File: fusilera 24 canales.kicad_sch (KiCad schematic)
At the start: 25 parts, among them Q2 MMBT2222A, Q3 MMBT2222A, U4 74HC132D, U5 LM339D, U6 BTS50010-1TAD

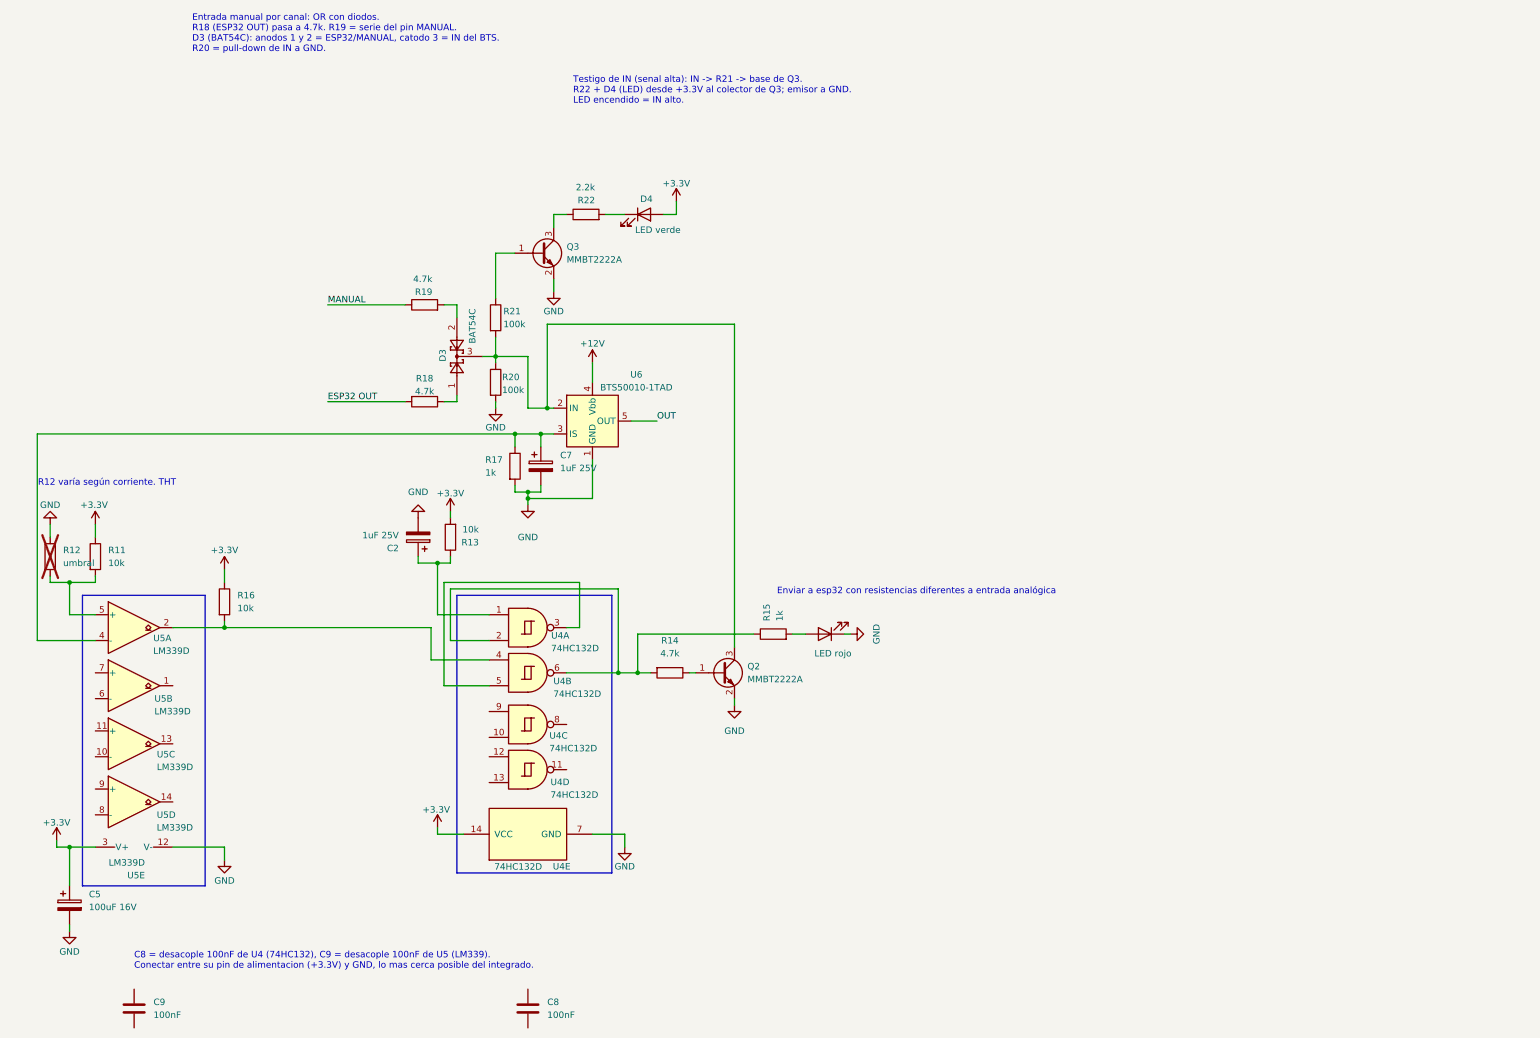
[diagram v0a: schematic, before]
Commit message: Añade ESP32 devkit, MCP23017 y biblioteca propia; renumera y documenta
- Esquemático anotado (referencias renumeradas), desacoples C2/C4 cableados
  y etiquetas de red para reducir cableado.
- Coloca el MCP23017 (SOIC-28W) y el ESP32 devkit V1 de 30 pines, ambos sin cablear.
- Biblioteca del proyecto en libs/: símbolo ESP32_DevKit_30pin y huella
  ESP32_DevKit_30pin_Socket (zócalos 2x15, 25,4 mm entre filas), con sym-lib-table
  y fp-lib-table.
- CONTEXTO_PROYECTO.md regenerado con las referencias actuales y la asignación
  de pines del ESP32 y el MCP23017.
- CLAUDE.md con las reglas de trabajo del repositorio.
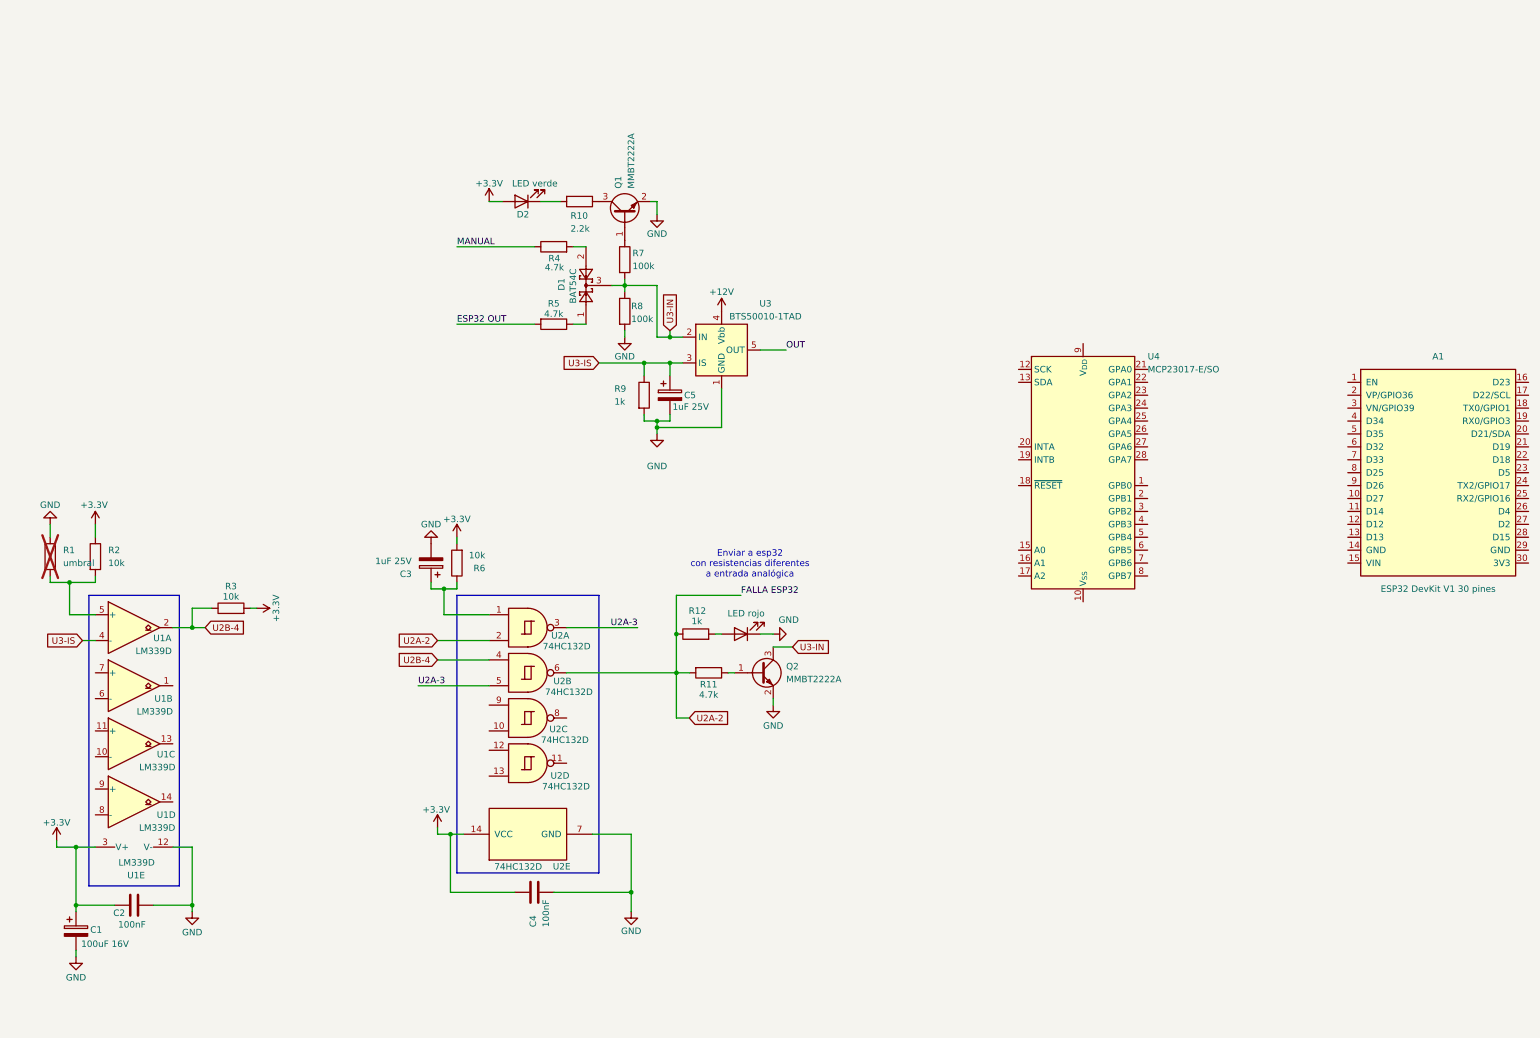
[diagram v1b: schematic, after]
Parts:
- added A1: ESP32 DevKit V1 30 pines, fusilera:ESP32_DevKit_30pin_Socket, symbol fusilera:ESP32_DevKit_30pin
- added U4: MCP23017-E/SO, Package_SO:SOIC-28W_7.5x17.9mm_P1.27mm, symbol Interface_Expansion:MCP23017x-x-SO
- renumbered C5 to C1, C9 to C2, C2 to C3, C8 to C4, C7 to C5, D3 to D1, D4 to D2, D2 to D3, Q3 to Q1, R12 to R1, R22 to R10, R14 to R11, R15 to R12, R11 to R2, R16 to R3, R19 to R4, R18 to R5, R13 to R6, R21 to R7, R20 to R8, R17 to R9, U5 to U1, U4 to U2, U6 to U3
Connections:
- net +3.3V: now also C2.1, C4.1, R3.2; no longer R3.1
- net GND: now also C2.2, C4.2
- net U3-IS: now reaches C5.1, R9.1, U1.4 (-), U3.3 (IS)
- net U3-IN: now reaches D1.3, Q2.3 (C), R7.2, R8.1, U3.2 (IN)
- net U2B-4: now reaches U1.2, U2.4
- net U2B-4: now also R3.1; no longer R3.2
- net U2A-3: now reaches U2.3, U2.5
- net U2A-2: now reaches R11.2, R12.1, U2.2, U2.6
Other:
- note removed: "C8 = desacople 100nF de U4 (74HC132), C9 = desacople 100nF de U5 (LM339). Conectar entre su pin de alimentacion (+3.3V) y GND, lo mas cerca posible del integrado."
- note removed: "Entrada manual por canal: OR con diodos. R18 (ESP32 OUT) pasa a 4.7k. R19 = serie del pin MANUAL. D3 (BAT54C): anodos 1 y 2 = ESP32/MANUAL, catodo 3 = IN del BTS. R20 = pull-down de IN a GND."
- note removed: "R12 varía según corriente. THT"
- note removed: "Testigo de IN (senal alta): IN -> R21 -> base de Q3. R22 + D4 (LED) desde +3.3V al colector de Q3; emisor a GND. LED encendido = IN alto."
- moved on the sheet: C1, C2, C3, C4, C5, D1, D2, Q1, Q2, R10, R11, R12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

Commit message: Añade MCP23017 de fallas y bloque de alimentación con LM5164
- Segundo MCP23017 (U5, 0x21) con su desacople: lee las entradas de falla y
  aporta 2 salidas (GPA7/GPB7 solo salida). Se descarta la lectura analógica.
- Bloque de alimentación cableado, sin conectar al resto: borne +12V, fusible de
  lógica, diodo de polaridad inversa, TVS, buck 12→5 V con LM5164 (red de
  rizado Tipo 3), diodo hacia el devkit y LDO 5→3,3 V con AP2112K.
- Puntos de conexión etiquetados: VBB, GND_PWR, VIN_ESP32 y V3V3_OUT.
- CONTEXTO_PROYECTO.md actualizado: reparto de pines, datos del datasheet del
  BTS, cobre para 40-50 A, decisiones de alimentación y tabla del bloque.
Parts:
- added C10: 2.2nF 50V X7R, Capacitor_SMD:C_0805_2012Metric, symbol Device:C
- added C11: 22uF 16V X7R, Capacitor_SMD:C_1206_3216Metric, symbol Device:C
- added C12: 1nF, Capacitor_SMD:C_0805_2012Metric, symbol Device:C
- added C13: 82pF C0G, Capacitor_SMD:C_0805_2012Metric, symbol Device:C
- added C14, C15: 1uF, Capacitor_SMD:C_0805_2012Metric, symbol Device:C
- added C6: 100nF, Capacitor_SMD:C_0805_2012Metric, symbol Device:C
- added C7, C8: 2.2uF 100V X7R, Capacitor_SMD:C_1210_3225Metric, symbol Device:C
- added C9: 47uF 50V, Capacitor_SMD:CP_Elec_8x10, symbol Device:C_Polarized
- added D4: SS36, Diode_SMD:D_SMB, symbol Device:D_Schottky
- added D5: SMBJ, Diode_SMD:D_SMB, symbol Device:D_Zener
- added D6: Schottky 1A (SS14), Diode_SMD:D_SMA, symbol Device:D_Schottky
- added F2: 2A, Fuse:Fuse_1206_3216Metric, symbol Device:Fuse
- added J1: +12V borne M6, MountingHole:MountingHole_6.4mm_M6_Pad, symbol Connector:Screw_Terminal_01x01
- added J2: GND borne M5, MountingHole:MountingHole_5.3mm_M5_Pad, symbol Connector:Screw_Terminal_01x01
- added L1: 22uH, Inductor_SMD:L_6.3x6.3_H3, symbol Device:L
- added R13: 301k, Resistor_SMD:R_0805_2012Metric, symbol Device:R
- added R14: 95.3k, Resistor_SMD:R_0805_2012Metric, symbol Device:R
- added R15: 31.6k, Resistor_SMD:R_0805_2012Metric, symbol Device:R
- added R16: 390k, Resistor_SMD:R_0805_2012Metric, symbol Device:R
- added R17: 1M, Resistor_SMD:R_0805_2012Metric, symbol Device:R
- added R18: 270k, Resistor_SMD:R_0805_2012Metric, symbol Device:R
- added U5: MCP23017-E/SO, Package_SO:SOIC-28W_7.5x17.9mm_P1.27mm, symbol Interface_Expansion:MCP23017x-x-SO
- added U6: LM5164DDA, Package_SO:HSOP-8-1EP_3.9x4.9mm_P1.27mm_EP2.41x3.1mm_ThermalVias, symbol Regulator_Switching:LM5164DDA
- added U7: AP2112K-3.3, Package_TO_SOT_SMD:SOT-23-5, symbol Regulator_Linear:AP2112K-3.3
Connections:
- new net: C7.1, C8.1, C9.1, D4.1 (K), D5.1 (K), R17.1, U6.2 (VIN)
- new net: R17.2, R18.1, U6.3 (EN/UVLO)
- new net: D4.2 (A), F2.2
- new net: R15.1, U6.4 (RON)
- new net: C11.1, C12.2, C14.1, D6.2 (A), L1.2, R13.1, U7.1 (VIN), U7.3 (EN)
- new net: C13.2, R13.2, R14.1, U6.5 (FB)
- new net: C10.1, U6.7 (BST)
- new net: C10.2, L1.1, R16.1, U6.8 (SW)
- new net: C12.1, C13.1, R16.2
- new net GND_PWR: C11.2, C14.2, C15.2, C7.2, C8.2, C9.2, D5.2 (A), J2.1 (Pin_1), R14.2, R15.2, R18.2, U6.1 (GND), U6.9 (EP), U7.2 (GND)
- new net V3V3_OUT: C15.1, U7.5 (VOUT)
- new net VBB: F2.1, J1.1 (Pin_1)
- new net VIN_ESP32: D6.1 (K)
- no-connect marks 0 -> 1
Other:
- note added: "30A maximo quitar fusible 19 salidas 9 directas con señal de error"
- note added: "PUNTOS DE CONEXION (etiquetas): VBB = Vbb de los BTS | GND_PWR = GND | VIN_ESP32 = VIN del devkit (A1 pin 15) | V3V3_OUT = +3.3V"
- note added: "U5 = 2.o MCP23017: lee las 16 entradas de falla (TRIP de cada canal), direccion 0x21 (A0 a 3.3V). C6 = desacople 100nF de U5. Las 8 fallas restantes irian a VP, VN, D34, D35 y 4 pines directos libres."

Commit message: Rutea el bloque de alimentación en el PCB de 4 capas y configura reglas
- Configura el PCB: stackup de 4 capas de 1,6 mm con cobre exterior de 2 oz,
  reglas de fabricación (0,2 mm, vías 0,6/0,3 mm) y clases de red para 10 A
  continuos (Potencia_12V, Entrada_Logica, Conmutacion, Potencia_5V_3V3).
- Importa los 53 footprints y rutea el bloque de alimentación en F.Cu
  (46 × 24 mm) siguiendo las reglas de layout del LM5164: CIN a 4,6 mm del VIN,
  divisor de realimentación junto al pin FB, SW a 6,2 mm de L1.
- Crea el plano de GND en In1 con 32 vías de 0,6/0,3 mm y uniones de 1 mm en
  los condensadores de entrada y salida y en el TVS (3 vías).
- Cambia la huella de U6 a la versión sin vías térmicas, en PCB y esquemático.
- DRC sin errores salvo el contorno de placa, que aún falta; el resto del
  circuito y los BTS siguen sin rutear.
- CONTEXTO_PROYECTO.md actualizado con el estado del PCB, el cálculo de cobre
  para 25-30 A en picos y la corriente continua de 10 A.
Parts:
- U6: footprint Package_SO:HSOP-8-1EP_3.9x4.9mm_P1.27mm_EP2.41x3.1mm_ThermalVias -> Package_SO:HSOP-8-1EP_3.9x4.9mm_P1.27mm_EP2.41x3.1mm
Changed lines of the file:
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@@
 			)
 		)
-		(property "Footprint" "Package_SO:HSOP-8-1EP_3.9x4.9mm_P1.27mm_EP2.41x3.1mm_ThermalVias"
+		(property "Footprint" "Package_SO:HSOP-8-1EP_3.9x4.9mm_P1.27mm_EP2.41x3.1mm"
 			(at 537.21 101.6 0)
 			(hide yes)

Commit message: Convierte los canales en una hoja jerárquica de celda con dos instancias
- Nueva hoja celda4.kicad_sch (4 canales, 1 LM339 y 2 × 74HC132) instanciada
  como Celda1 y Celda2 en la hoja principal; las referencias de la Celda2 son
  las de la Celda1 más 100.
- Etiquetas únicas por canal como pines de hoja (ESP32_OUT1-4, MANUAL1-4,
  OUT1-4, FALLA1-4): ya no se unen entre sí las salidas, las entradas ni las
  fallas de distintos canales.
- Añade los pull-ups de 10 k que faltaban en las salidas de los comparadores de
  los canales 3 y 4 (R53 y R54).
- Re-vincula en el PCB los 25 footprints existentes de la celda a la Celda1 para
  conservar su colocación.
- La huella de la ESP32 lleva los nombres de los pines en la serigrafía.
- CONTEXTO_PROYECTO.md actualizado: 28 canales (19 controlados y 9 siempre en
  alto), reparto de E/S sin tercer MCP y estructura jerárquica.
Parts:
- removed C1: 100uF 16V, Capacitor_SMD:CP_Elec_6.3x5.4, symbol Device:C_Polarized
- removed C2, C4: 100nF, Capacitor_SMD:C_0805_2012Metric, symbol Device:C
- removed C3, C5: 1uF 25V, Capacitor_SMD:CP_Elec_4x5.4, symbol Device:C_Polarized
- removed D1: BAT54C, Package_TO_SOT_SMD:SOT-23, symbol Diode:BAT54C
- removed D2: LED verde, LED_SMD:LED_0805_2012Metric, symbol Device:LED
- removed D3: LED rojo, LED_SMD:LED_0805_2012Metric, symbol Device:LED
- removed Q1, Q2: MMBT2222A, Package_TO_SOT_SMD:SOT-23, symbol Transistor_BJT:MMBT2222A
- removed R1: umbral, Resistor_THT:R_Axial_DIN0207_L6.3mm_D2.5mm_P10.16mm_Horizontal, symbol Device:R
- removed R10: 2.2k, Resistor_SMD:R_0805_2012Metric, symbol Device:R
- removed R11, R4, R5: 4.7k, Resistor_SMD:R_0805_2012Metric, symbol Device:R
- removed R12, R9: 1k, Resistor_SMD:R_0805_2012Metric, symbol Device:R
- removed R2, R3, R6: 10k, Resistor_SMD:R_0805_2012Metric, symbol Device:R
- removed R7, R8: 100k, Resistor_SMD:R_0805_2012Metric, symbol Device:R
- removed U1: LM339D, Package_SO:SOIC-14_3.9x8.7mm_P1.27mm, symbol Comparator:LM339
- removed U2: 74HC132D, Package_SO:SOIC-14_3.9x8.7mm_P1.27mm, symbol 74xx:74LS132
- removed U3: BTS50010-1TAD, Package_TO_SOT_SMD:TO-263-7_TabPin4, symbol Power_Management:BTS50010-1TAD
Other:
- added sheet Celda1 (celda4.kicad_sch)
- added sheet Celda2 (celda4.kicad_sch)
- note added: "POWER"
- note removed: "Enviar a esp32 con resistencias diferentes a entrada analógica"
- moved on the sheet: A1, C10, C11, C12, C13, C14, C15, C6, C7, C8, C9, D4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

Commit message: Importa las dos celdas al PCB y avanza el ruteo de la Celda1
- Importa a la placa los 202 footprints (bloque de alimentación, ESP32, MCP23017
  y las celdas Celda1 y Celda2); paridad con el esquemático sin problemas.
- Avanza el ruteo: 371 segmentos y 43 vías; el plano de GND de In1 se mantiene.
- Reubica en el esquemático el grupo del ESP32 y los MCP23017.
- El DRC sigue marcando el contorno que falta, 260 conexiones por rutear y
  18 avisos de espaciado pendientes de revisar.
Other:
- moved on the sheet: A1, C6, U4, U5
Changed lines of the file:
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@@
 	(text "U5 = 2.o MCP23017: lee las 16 entradas de falla (TRIP de cada canal), direccion 0x21 (A0 a 3.3V).\nC6 = desacople 100nF de U5. Las 8 fallas restantes irian a VP, VN, D34, D35 y 4 pines directos libres."
 		(exclude_from_sim no)
-		(at 236.22 247.65 0)
+		(at 600.71 504.19 0)
 		(effects
 			(font
@@
 	(symbol
 		(lib_id "Device:C")
-		(at 236.22 307.34 0)
+		(at 600.71 563.88 0)
 		(unit 1)
 		(body_style 1)
@@
 		(dnp no)
 		(property "Reference" "C6"
-			(at 240.03 306.07 0)
+			(at 604.52 562.61 0)
 			(show_name no)
 			(do_not_autoplace no)
@@
 		)
 		(property "Value" "100nF"
-			(at 240.03 308.61 0)
+			(at 604.52 565.15 0)
 			(show_name no)
 			(do_not_autoplace no)
@@
 		)
 		(property "Footprint" "Capacitor_SMD:C_0805_2012Metric"
-			(at 236.22 307.34 0)
+			(at 600.71 563.88 0)
 			(hide yes)
 			(show_name no)
@@
 		)
 		(property "Datasheet" "~"
-			(at 236.22 307.34 0)
+			(at 600.71 563.88 0)
 			(hide yes)
 			(show_name no)
@@
 		)
 		(property "Description" "Unpolarized capacitor"
-			(at 236.22 307.34 0)
+			(at 600.71 563.88 0)
 			(hide yes)
 			(show_name no)
@@
 	(symbol
 		(lib_id "Interface_Expansion:MCP23017x-x-SO")
-		(at 236.22 275.59 0)
+		(at 600.71 532.13 0)
 		(unit 1)
 		(body_style 1)
@@
 		(dnp no)
 		(property "Reference" "U5"
-			(at 248.92 251.46 0)
+			(at 613.41 508 0)
 			(show_name no)
 			(do_not_autoplace no)
@@
 		)
 		(property "Value" "MCP23017-E/SO"
-			(at 248.92 254 0)
+			(at 613.41 510.54 0)
 			(show_name no)
 			(do_not_autoplace no)
@@
 		)
 		(property "Footprint" "Package_SO:SOIC-28W_7.5x17.9mm_P1.27mm"
-			(at 236.22 275.59 0)
+			(at 600.71 532.13 0)
 			(hide yes)
 			(show_name no)
@@
 		)
 		(property "Datasheet" "https://ww1.microchip.com/downloads/aemDocuments/documents/APID/ProductDocuments/DataSheets/MCP23017-Data-Sheet-DS20001952.pdf"
-			(at 236.22 275.59 0)
+			(at 600.71 532.13 0)
 			(hide yes)
 			(show_name no)
@@
 		)
 		(property "Description" "16-bit I/O expander, I2C, interrupts, w pull-ups, GPA7/GPB7 output only (https://microchip.my.site.com/s/article/GPA7---GPB7-Cannot-Be-Used-as-Inputs-In-MCP23017),  SOIC-28"
-			(at 236.22 275.59 0)
+			(at 600.71 532.13 0)
 			(hide yes)
 			(show_name no)
@@
 	(symbol
 		(lib_id "fusilera:ESP32_DevKit_30pin")
-		(at 306.07 210.82 0)
+		(at 670.56 467.36 0)
 		(unit 1)
 		(body_style 1)
@@
 		(dnp no)
 		(property "Reference" "A1"
-			(at 306.07 187.96 0)
+			(at 670.56 444.5 0)
 			(show_name no)
 			(do_not_autoplace no)
@@
 		)
 		(property "Value" "ESP32 DevKit V1 30 pines"
-			(at 306.07 233.68 0)
+			(at 670.56 490.22 0)
 			(show_name no)
 			(do_not_autoplace no)
@@
 		)
 		(property "Footprint" "fusilera:ESP32_DevKit_30pin_Socket"
-			(at 306.07 210.82 0)
+			(at 670.56 467.36 0)
 			(hide yes)
 			(show_name no)
@@
 		)
 		(property "Datasheet" "~"
-			(at 306.07 210.82 0)
+			(at 670.56 467.36 0)
 			(hide yes)
 			(show_name no)
@@
 		)
 		(property "Description" "ESP32 DevKit V1 (30 pines) en zocalos 2x15. Pines 1-15 columna izquierda (arriba a abajo), 16-30 columna derecha (arriba a abajo), USB abajo"
-			(at 306.07 210.82 0)
+			(at 670.56 467.36 0)
 			(hide yes)
 			(show_name no)
@@
 	(symbol
 		(lib_id "Interface_Expansion:MCP23017x-x-SO")
-		(at 236.22 210.82 0)
+		(at 600.71 467.36 0)
 		(unit 1)
 		(body_style 1)
@@
 		(dnp no)
 		(property "Reference" "U4"
-			(at 248.92 187.96 0)
+			(at 613.41 444.5 0)
 			(show_name no)
 			(do_not_autoplace no)
@@
 		)
 		(property "Value" "MCP23017-E/SO"
-			(at 248.92 190.5 0)
+			(at 613.41 447.04 0)
 			(show_name no)
 			(do_not_autoplace no)
@@
 		)
 		(property "Footprint" "Package_SO:SOIC-28W_7.5x17.9mm_P1.27mm"
-			(at 236.22 210.82 0)
+			(at 600.71 467.36 0)
 			(hide yes)
 			(show_name no)
@@
 		)
 		(property "Datasheet" "https://ww1.microchip.com/downloads/aemDocuments/documents/APID/ProductDocuments/DataSheets/MCP23017-Data-Sheet-DS20001952.pdf"
-			(at 236.22 210.82 0)
+			(at 600.71 467.36 0)
 			(hide yes)
 			(show_name no)
@@
 		)
 		(property "Description" "16-bit I/O expander, I2C, interrupts, w pull-ups, GPA7/GPB7 output only (https://microchip.my.site.com/s/article/GPA7---GPB7-Cannot-Be-Used-as-Inputs-In-MCP23017),  SOIC-28"
-			(at 236.22 210.82 0)
+			(at 600.71 467.36 0)
 			(hide yes)
 			(show_name no)

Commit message: Une GND_PWR con GND y añade el plano de +3,3 V en In2
Sustituye las tres etiquetas GND_PWR del esquemático raíz por símbolos de
tierra para que el bloque de poder comparta la red GND con las celdas. El
plano de In1 pasa a la red GND y se añade el plano de +3,3 V en In2 sobre la
Celda1. Continúa el ruteo de la Celda1 (más vías y pistas en F.Cu e In2) y se
actualiza CONTEXTO_PROYECTO.md.
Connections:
- net GND_PWR renamed GND
